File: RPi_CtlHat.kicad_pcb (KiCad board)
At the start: 2 copper layers, 65 x 56.5 mm, 44 parts, among them J1 RPi_GPIO, P1 CONN_01X02, P2 DIL10, U1 MCP1754ST-3302E/MB, U2 MCP2515, U3 MCP2551, U4 74HCT541_PWR, U5 PCA9306D, Y1 16MHz

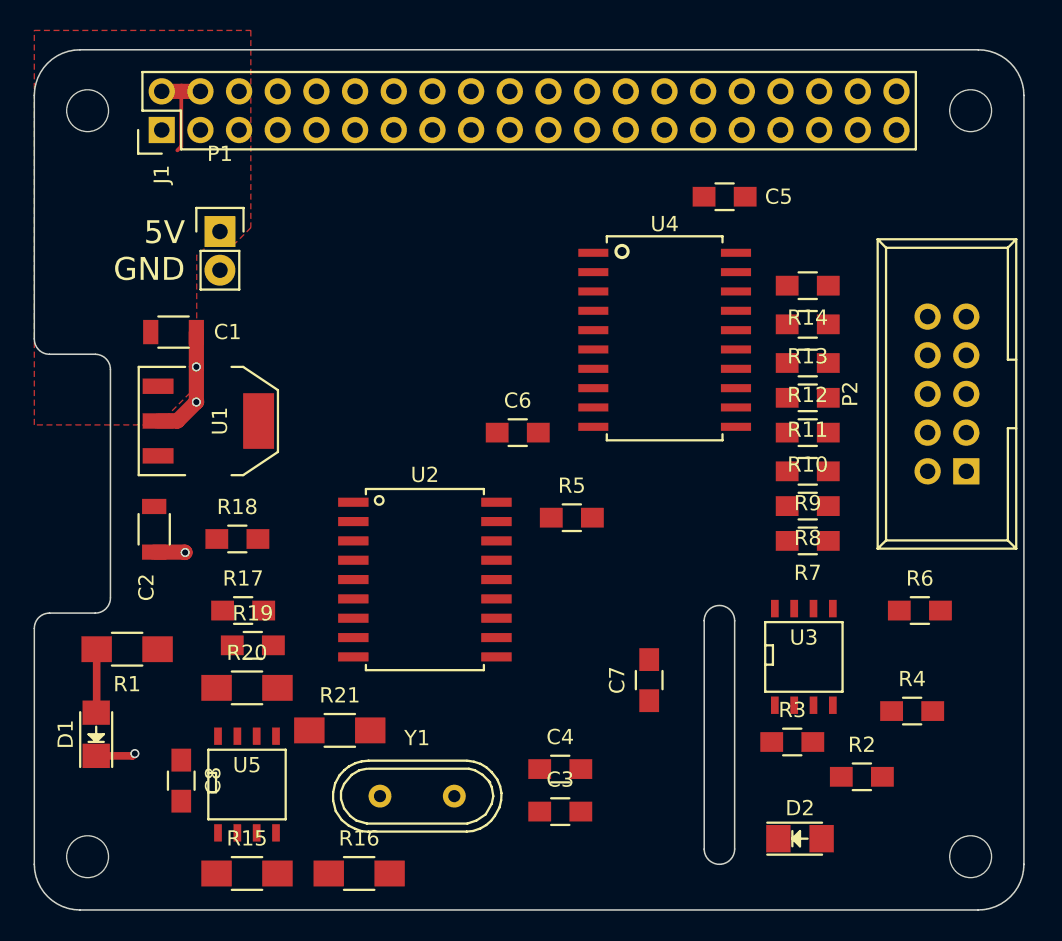
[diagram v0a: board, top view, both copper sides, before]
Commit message: First fully routed pcb
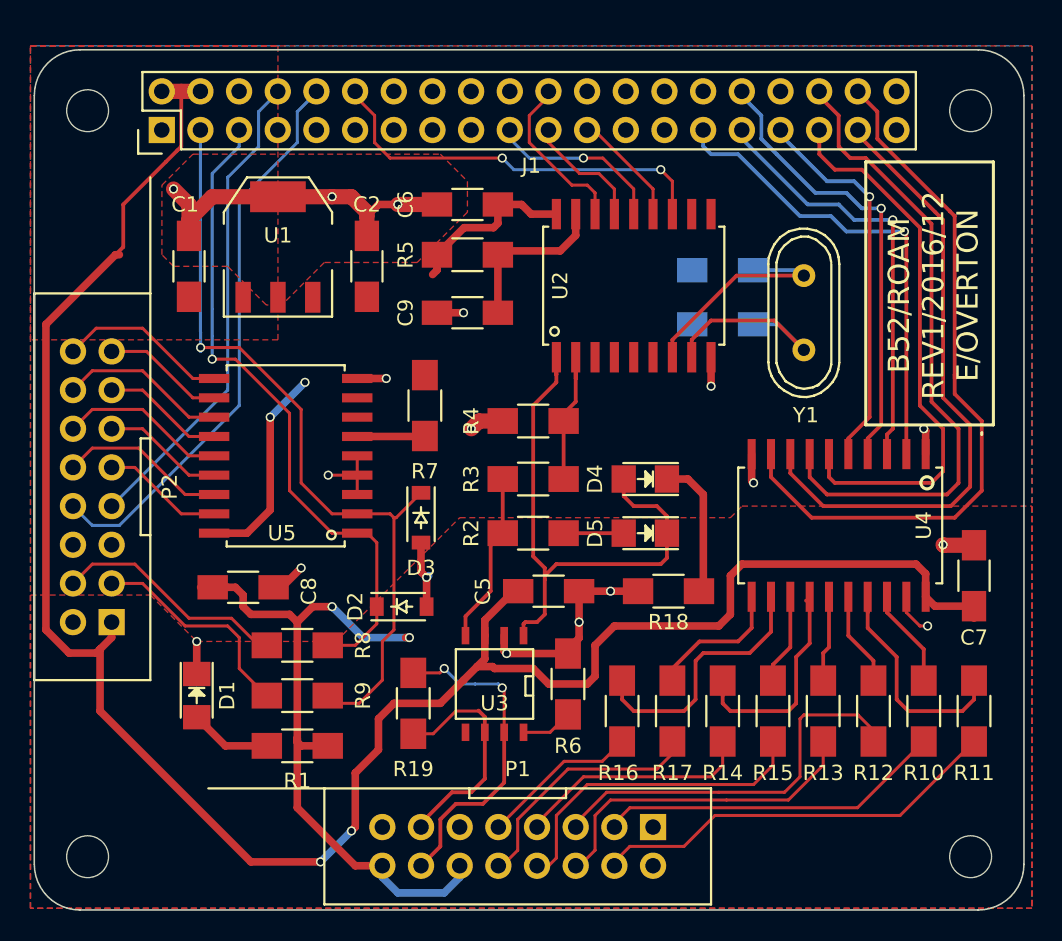
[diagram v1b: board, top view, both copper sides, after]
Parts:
- removed R20, R21: 100R, Resistors_SMD:R_1206_HandSoldering
- added C9: ?n, Capacitors_SMD:C_1206_HandSoldering, F.Cu at (123.7, 64.3)
- added D3: 3.3v, Diodes_SMD:SOD-123, F.Cu at (120.7, 77.7)
- added D4: LED, LEDs:LED_1206, F.Cu at (135.4, 75.2)
- added D5: LED, LEDs:LED_1206, F.Cu at (135.4, 78.7)
- C1, C2: footprint Capacitors_SMD:C_1206 -> Capacitors_SMD:C_1206_HandSoldering
- C3, C4: footprint Resistors_SMD:R_0805_HandSoldering -> Capacitors_SMD:C_1206_HandSoldering; moved to B.Cu
- C5, C6, C7, C8: footprint Resistors_SMD:R_0805_HandSoldering -> Capacitors_SMD:C_1206_HandSoldering
- D2: value LED -> 3.3v; footprint LEDs:LED_1206 -> Diodes_SMD:SOD-123
- P1: value CONN_01X02 -> CONN_02X08; footprint Pin_Headers:Pin_Header_Straight_1x02 -> components:D300_16
- P2: value DIL10 -> CONN_02X08; footprint Connect:IDC_Header_Straight_10pins -> components:D300_16
- R10, R11, R12, R13, R14, R2, R3, R4, R5, R6, R8, R9: footprint Resistors_SMD:R_0805_HandSoldering -> Resistors_SMD:R_1206_HandSoldering
- R17: value 200k -> 100R; footprint Resistors_SMD:R_0805_HandSoldering -> Resistors_SMD:R_1206_HandSoldering
- R18: value 1k -> 200R; footprint Resistors_SMD:R_0805_HandSoldering -> Resistors_SMD:R_1206_HandSoldering
- R19: value 1k -> 120R; footprint Resistors_SMD:R_0805_HandSoldering -> Resistors_SMD:R_1206_HandSoldering
- R7: value 100R -> 4k7; footprint Resistors_SMD:R_0805_HandSoldering -> Resistors_SMD:R_1206_HandSoldering
- U5: value PCA9306D -> MCP23008; footprint SMD_Packages:SOIC-8-N -> components:SOIC-18
- moved P2 54.9 mm to (101.6, 75.7)
- moved P1 42.6 mm to (127.0, 96.8), turned to 180 degrees
- moved Y1 40.7 mm to (145.8, 64.3), turned to 270 degrees
- moved R9 36.6 mm to (112.5, 89.4), turned to 0 degrees
- moved R15 36.2 mm to (143.8, 90.4), turned to 90 degrees
- moved R8 34.8 mm to (112.5, 86.1), turned to 0 degrees
- moved C4 34.5 mm to (140.5, 61.5), turned to 180 degrees
- moved C3 33.7 mm to (140.5, 65.0), turned to 180 degrees
- moved R4 31.3 mm to (128.0, 71.4), turned to 180 degrees
- moved D2 30.3 mm to (119.4, 83.6)
- moved R17 29.0 mm to (137.2, 90.4), turned to 90 degrees
- moved R18 28.5 mm to (136.9, 82.5)
- moved R14 28.5 mm to (140.5, 90.4), turned to 90 degrees
- moved C5 28.4 mm to (129.0, 82.5)
- moved R2 26.9 mm to (128.0, 78.7)
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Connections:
- C8 pad 1: Net-(C8-Pad1) -> VCC
- D2 pad 1: GND -> /SCL1
- D2 pad 2: Net-(D2-Pad2) -> GND
- J1 pad 10: Net-(J1-Pad10) -> /GPIO15RX
- J1 pad 8: Net-(J1-Pad8) -> /GPIO14TX
- P1 pad 1: +5V -> GND
- P1 pad 2: GND -> +5V
- P2 pad 1: GND -> +5V
- P2 pad 10: +5V -> /XGPIO6
- P2 pad 2: /PWM0_OUT -> GND
- P2 pad 3: /PWM1_OUT -> /SDA1B
- P2 pad 4: /PWM2_OUT -> /SCL1B
- P2 pad 5: /PWM3_OUT -> VCC
- P2 pad 6: /PWM4_OUT -> GND
- P2 pad 7: /PWM5_OUT -> /GPIO14TX
- P2 pad 8: /PWM6_OUT -> /GPIO15RX
- P2 pad 9: /PWM7_OUT -> /XGPIO7
- R10 pad 1: /PWM6_OUT -> /PWM0_OUT
- R12 pad 1: /PWM3_OUT -> /PWM2_OUT
- R13 pad 1: /PWM5_OUT -> /PWM3_OUT
- R14 pad 1: /PWM7_OUT -> /PWM4_OUT
- R15 pad 1: /SCL1_3 -> /PWM5_OUT
- R15 pad 2: /SCL1 -> Net-(R15-Pad2)
- R16 pad 1: /SDA1_3 -> /PWM6_OUT
- R16 pad 2: /SDA1 -> Net-(R16-Pad2)
- R17 pad 1: Net-(C8-Pad1) -> /PWM7_OUT
- R17 pad 2: +5V -> Net-(R17-Pad2)
- R18 pad 1: Net-(D5-Pad1) -> GND
- R18 pad 2: +5V -> Net-(D4-Pad1)
- R19 pad 1: Net-(D6-Pad1) -> /CANL
- R19 pad 2: +5V -> /CANH
- R2 pad 2: Net-(D2-Pad2) -> Net-(D5-Pad2)
- R7 pad 1: /PWM0_OUT -> Net-(R7-Pad1)
- R7 pad 2: Net-(R7-Pad2) -> VCC
- R8 pad 1: /PWM2_OUT -> /SCL1B
- R8 pad 2: Net-(R8-Pad2) -> /SCL1
- R9 pad 1: /PWM4_OUT -> /SDA1B
- R9 pad 2: Net-(R9-Pad2) -> /SDA1
- U1 pad 4: (no net) -> GND
- U3 pad 6: Net-(U3-Pad6) -> /CANL
- U3 pad 7: Net-(U3-Pad7) -> /CANH
- U4 pad 1: Net-(U4-Pad1) -> GND
- U4 pad 11: Net-(R14-Pad2) -> Net-(R17-Pad2)
- U4 pad 12: Net-(R10-Pad2) -> Net-(R16-Pad2)
- U4 pad 13: Net-(R13-Pad2) -> Net-(R15-Pad2)
- U4 pad 14: Net-(R9-Pad2) -> Net-(R14-Pad2)
- U4 pad 15: Net-(R12-Pad2) -> Net-(R13-Pad2)
- U4 pad 16: Net-(R8-Pad2) -> Net-(R12-Pad2)
- U4 pad 18: Net-(R7-Pad2) -> Net-(R10-Pad2)
- U4 pad 19: Net-(U4-Pad19) -> GND
- U5 pad 1: GND -> /SCL1
- U5 pad 2: VCC -> /SDA1
- U5 pad 3: /SCL1 -> GND
- U5 pad 4: /SDA1 -> GND
- U5 pad 5: Net-(D6-Pad1) -> GND
- U5 pad 6: Net-(D5-Pad1) -> Net-(R7-Pad1)
- U5 pad 7: Net-(C8-Pad1) -> Net-(U5-Pad7)
- U5 pad 8: Net-(C8-Pad1) -> Net-(U5-Pad8)
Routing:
- net +5V: track 9.31 -> 141.4 mm, vias 0 -> 2
- net VCC: track 0.03 -> 72.2 mm, vias 0 -> 4
- net GND: track 12.3 -> 69.9 mm, vias 4 -> 18
- net /SDA1: track 0.05 -> 53.9 mm, vias 0 -> 1
- net /PWM7: track 0.00 -> 48.1 mm
- net /SCL1: track 0.00 -> 43.8 mm, vias 0 -> 1
- net /PWM5: track 0.00 -> 42.5 mm
- net /PWM6: track 0.00 -> 41.2 mm
- net /PWM4: track 0.00 -> 37.7 mm
- net /GPIO15RX: track 0.00 -> 37.4 mm
- net /CAN0_TXCAN: track 0.00 -> 36.1 mm
- net /GPIO14TX: track 0.00 -> 31.8 mm
- net /PWM0: track 0.00 -> 31.3 mm, vias 0 -> 1
- net /PWM2: track 0.00 -> 29.9 mm, vias 0 -> 1
- net /PWM1: track 0.00 -> 28.5 mm, vias 0 -> 1
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- added copper zone on B.Cu, net GND
- added copper zone on F.Cu, net GND
- added copper zone on F.Cu, net VCC
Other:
- outline, holes or cut-outs redrawn
- board text added: "B52/ROAM REV1/2016/12 E/OVERTON"
- board text removed: "5V GND"
